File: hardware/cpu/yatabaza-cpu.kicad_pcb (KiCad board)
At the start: 2 copper layers, 46.4 x 60.3 mm, 28 parts, among them P1 SCREW, P10 uSD, P11 HOST, P12 KEYBOARD, P13 MIDI, P2 SCREW, P3 BUS, P4 POWER, P5 SUPPORT, P7 RTC, P8 PANEL, P9 LD, U1 STM32F103 BLUE PILL, U2 74HCT04, U3 6N138

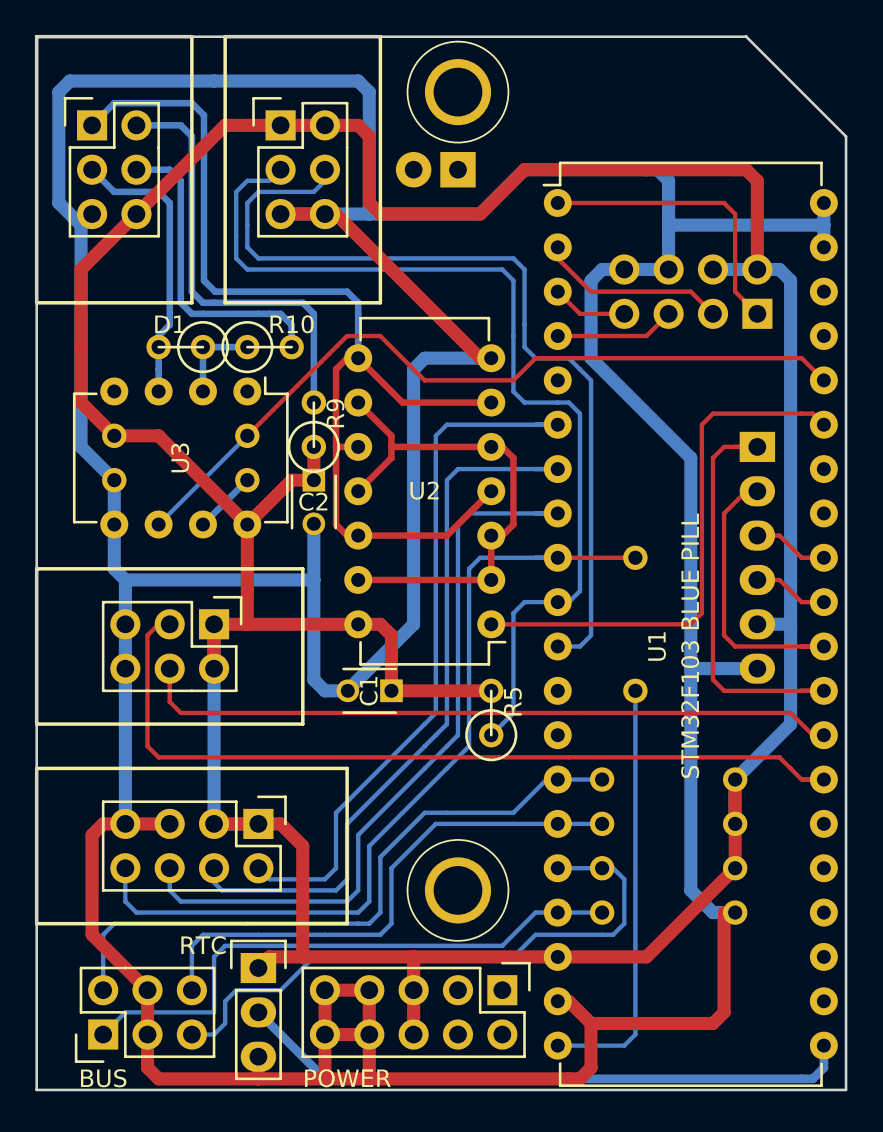
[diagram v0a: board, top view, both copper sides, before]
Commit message: ~ Ported hardware to Kicad6
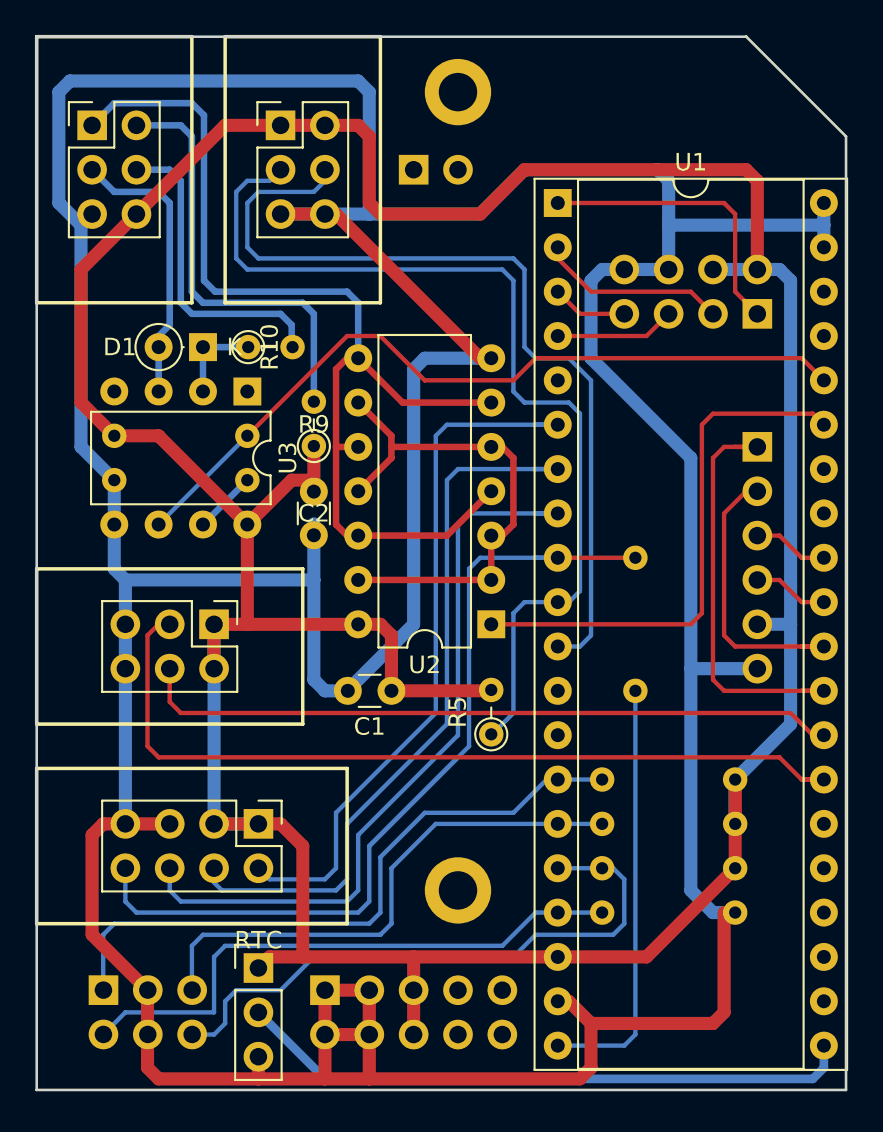
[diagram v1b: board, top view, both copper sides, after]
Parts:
- C1, C2: footprint Capacitors_ThroughHole:C_Disc_D3_P2.5 -> Capacitor_THT:C_Disc_D3.0mm_W1.6mm_P2.50mm
- D1: footprint Discret:R1 -> Diode_THT:D_DO-35_SOD27_P2.54mm_Vertical_KathodeUp
- P1, P2: footprint digikey-footprints:Test-Point-Pin_Drill2.79mm -> MountingHole:MountingHole_2.2mm_M2_ISO14580_Pad
- P10: footprint Pin_Headers:Pin_Header_Straight_1x06 -> Connector_PinHeader_2.54mm:PinHeader_1x06_P2.54mm_Vertical
- P11: footprint Pin_Headers:Pin_Header_Straight_2x04 -> Connector_PinHeader_2.54mm:PinHeader_2x04_P2.54mm_Vertical
- P12: footprint Pin_Headers:Pin_Header_Angled_2x04 -> Connector_PinHeader_2.54mm:PinHeader_2x04_P2.54mm_Horizontal
- P13, P8, P9: footprint Pin_Headers:Pin_Header_Straight_2x03 -> Connector_PinHeader_2.54mm:PinHeader_2x03_P2.54mm_Vertical
- P3: footprint Pin_Headers:Pin_Header_Straight_2x03 -> Connector_PinHeader_2.54mm:PinHeader_2x03_P2.54mm_Vertical; moved to B.Cu
- P4: footprint Pin_Headers:Pin_Header_Straight_2x05 -> Connector_PinHeader_2.54mm:PinHeader_2x05_P2.54mm_Vertical; moved to B.Cu
- P5: footprint Pin_Headers:Pin_Header_Straight_1x02 -> Connector_PinHeader_2.54mm:PinHeader_1x02_P2.54mm_Vertical
- P7: footprint Pin_Headers:Pin_Header_Straight_1x03 -> Connector_PinHeader_2.54mm:PinHeader_1x03_P2.54mm_Vertical
- R1, R2, R3, R4, R6, R7, R8: footprint Discret:R3 -> Resistor_THT:R_Axial_DIN0204_L3.6mm_D1.6mm_P7.62mm_Horizontal
- R10, R5, R9: footprint Discret:R1 -> Resistor_THT:R_Axial_DIN0204_L3.6mm_D1.6mm_P2.54mm_Vertical
- U1: footprint Housings_DIP:DIP-40_W15.24mm -> Package_DIP:DIP-40_W15.24mm_Socket
- U2: footprint Housings_DIP:DIP-14_W7.62mm -> Package_DIP:DIP-14_W7.62mm
- U3: footprint Housings_DIP:DIP-8_W7.62mm -> Package_DIP:DIP-8_W7.62mm
- moved P4 10.2 mm to (31.1, 66.7)
- moved R2 3.81 mm to (54.6, 62.2)
- moved R6 3.81 mm to (48.9, 41.9)
- moved R7 3.81 mm to (19.1, 34.9)
- moved R8 3.81 mm to (19.1, 37.5)
- moved R1 3.81 mm to (47.0, 59.7)
- moved R3 3.81 mm to (47.0, 57.1)
- moved R4 3.81 mm to (47.0, 54.6)
- moved P3 2.55 mm to (18.4, 66.7), turned to -90 degrees
- moved P5 2.54 mm to (36.2, 19.7), turned to -90 degrees
- moved D1 1.27 mm to (24.1, 29.8)
- moved R5 1.22 mm to (40.6, 52.0)
- moved R10 1.22 mm to (26.7, 29.8)
- moved R9 1.22 mm to (30.5, 35.5)
- moved C2 0.65 mm to (30.5, 38.1)
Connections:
- net /VBAT renamed +BATT
- net /~KBD_LD renamed /~{KBD_LD}
- net /~SD_SS renamed /~{SD_SS}
- P1 pad 1: Net-(P1-Pad1) -> unconnected-(P1-Pad1)
- P2 pad 1: Net-(P2-Pad1) -> unconnected-(P2-Pad1)
- P3 pad 1: /~RST -> /SCL
- P3 pad 2: /SCL -> /~{RST}
- P3 pad 5: /~IRQ -> /SDA
- P3 pad 6: /SDA -> /~{IRQ}
- P4 pad 1: Net-(P4-Pad1) -> GND
- P4 pad 10: GND -> unconnected-(P4-Pad10)
- P4 pad 2: Net-(P4-Pad2) -> GND
- P4 pad 3: Net-(P4-Pad3) -> GND
- P4 pad 4: Net-(P4-Pad4) -> GND
- P4 pad 7: GND -> unconnected-(P4-Pad7)
- P4 pad 8: GND -> unconnected-(P4-Pad8)
- P4 pad 9: GND -> unconnected-(P4-Pad9)
- P5 pad 1: Net-(P5-Pad1) -> unconnected-(P5-Pad1)
- P5 pad 2: Net-(P5-Pad2) -> unconnected-(P5-Pad2)
- R1 pad 1: /~IRQ -> /~{IRQ}
- R2 pad 2: /~RST -> /~{RST}
- U1 pad 12: Net-(U1-Pad12) -> unconnected-(U1-Pad12)
- U1 pad 13: Net-(U1-Pad13) -> unconnected-(U1-Pad13)
- U1 pad 16: /~IRQ -> /~{IRQ}
- U1 pad 17: /~RST -> /~{RST}
- U1 pad 22: Net-(U1-Pad22) -> unconnected-(U1-Pad22)
- U1 pad 23: Net-(U1-Pad23) -> unconnected-(U1-Pad23)
- U1 pad 24: Net-(U1-Pad24) -> unconnected-(U1-Pad24)
- U1 pad 25: Net-(U1-Pad25) -> unconnected-(U1-Pad25)
- U1 pad 26: Net-(U1-Pad26) -> unconnected-(U1-Pad26)
- U1 pad 33: Net-(U1-Pad33) -> unconnected-(U1-Pad33)
- U1 pad 34: Net-(U1-Pad34) -> unconnected-(U1-Pad34)
- U1 pad 37: Net-(U1-Pad37) -> unconnected-(U1-Pad37)
- U1 pad 38: Net-(U1-Pad38) -> unconnected-(U1-Pad38)
- U1 pad 5: Net-(U1-Pad5) -> unconnected-(U1-Pad5)
- U3 pad 1: (no net) -> unconnected-(U3-Pad1)
- U3 pad 4: (no net) -> unconnected-(U3-Pad4)
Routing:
- net /~IRQ: track 36.0 -> 0.00 mm
- net /~{IRQ}: track 0.00 -> 34.8 mm
- net /~{RST}: track 0.00 -> 32.7 mm
- net /~RST: track 32.7 -> 0.00 mm
- net /USBD+: track 48.9 -> 56.1 mm
- net /LD_RX: track 51.6 -> 49.7 mm
- net /LD_TX: track 56.0 -> 54.7 mm
- net GND: track 301.3 -> 300.4 mm
- net Net-(D1-Pad2): track 16.9 -> 16.3 mm
- net Net-(P13-Pad1): track 60.4 -> 59.8 mm
- net /USBD-: track 43.2 -> 42.5 mm
- net /SD_CK: track 16.0 -> 15.4 mm
- net Net-(U2-Pad11): track 30.0 -> 29.4 mm
- net /KBD_CK: track 10.8 -> 10.2 mm
- net /SDA: track 30.8 -> 30.2 mm
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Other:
- net class Default removed
- rule pad_to_mask_clearance: 0.2 -> 0
